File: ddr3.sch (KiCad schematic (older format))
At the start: 36 parts, among them U7 AS4C256M16D3, U8 TPS51200DRC

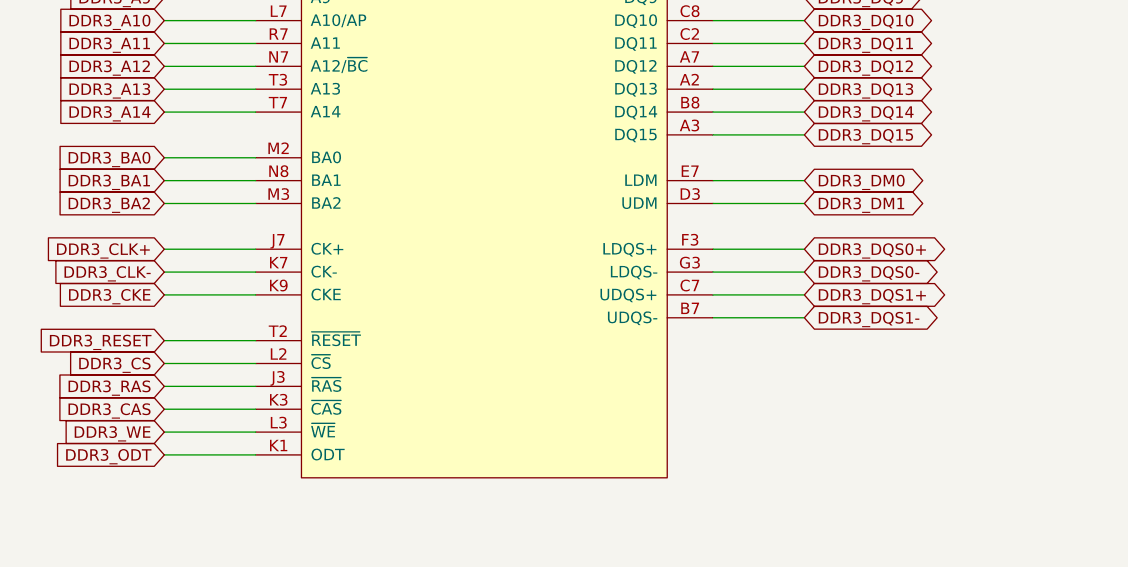
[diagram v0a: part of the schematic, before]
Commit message: DDR routing in progress
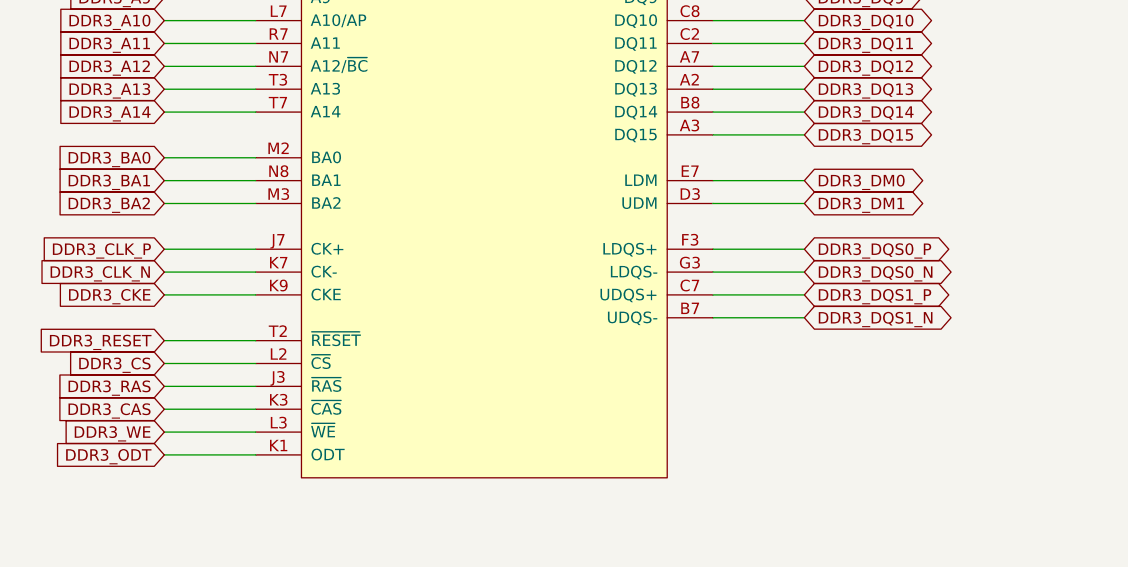
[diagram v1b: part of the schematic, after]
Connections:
- net DDR3_CLK+: no longer U7.J7 (CK+)
- net DDR3_CLK-: no longer U7.K7 (CK-)
- net DDR3_DQS0+ renamed DDR3_DQS0_P
- net DDR3_DQS0- renamed DDR3_DQS0_N
- net DDR3_DQS1+ renamed DDR3_DQS1_P
- net DDR3_DQS1- renamed DDR3_DQS1_N
- new net DDR3_CLK_N: U7.K7 (CK-)
- new net DDR3_CLK_P: U7.J7 (CK+)
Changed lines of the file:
@@
 DDR3_BA2
 Text GLabel 3650 4625 0    50   Input ~ 0
-DDR3_CLK+
+DDR3_CLK_P
 Text GLabel 3650 4725 0    50   Input ~ 0
-DDR3_CLK-
+DDR3_CLK_N
 Text GLabel 3650 4825 0    50   Input ~ 0
 DDR3_CKE
@@
 	6050 4425 6450 4425
 Text GLabel 6450 4625 2    50   BiDi ~ 0
-DDR3_DQS0+
+DDR3_DQS0_P
 Text GLabel 6450 4725 2    50   BiDi ~ 0
-DDR3_DQS0-
+DDR3_DQS0_N
 Text GLabel 6450 4825 2    50   BiDi ~ 0
-DDR3_DQS1+
+DDR3_DQS1_P
 Text GLabel 6450 4925 2    50   BiDi ~ 0
-DDR3_DQS1-
+DDR3_DQS1_N
 Wire Wire Line
 	6450 4625 6050 4625

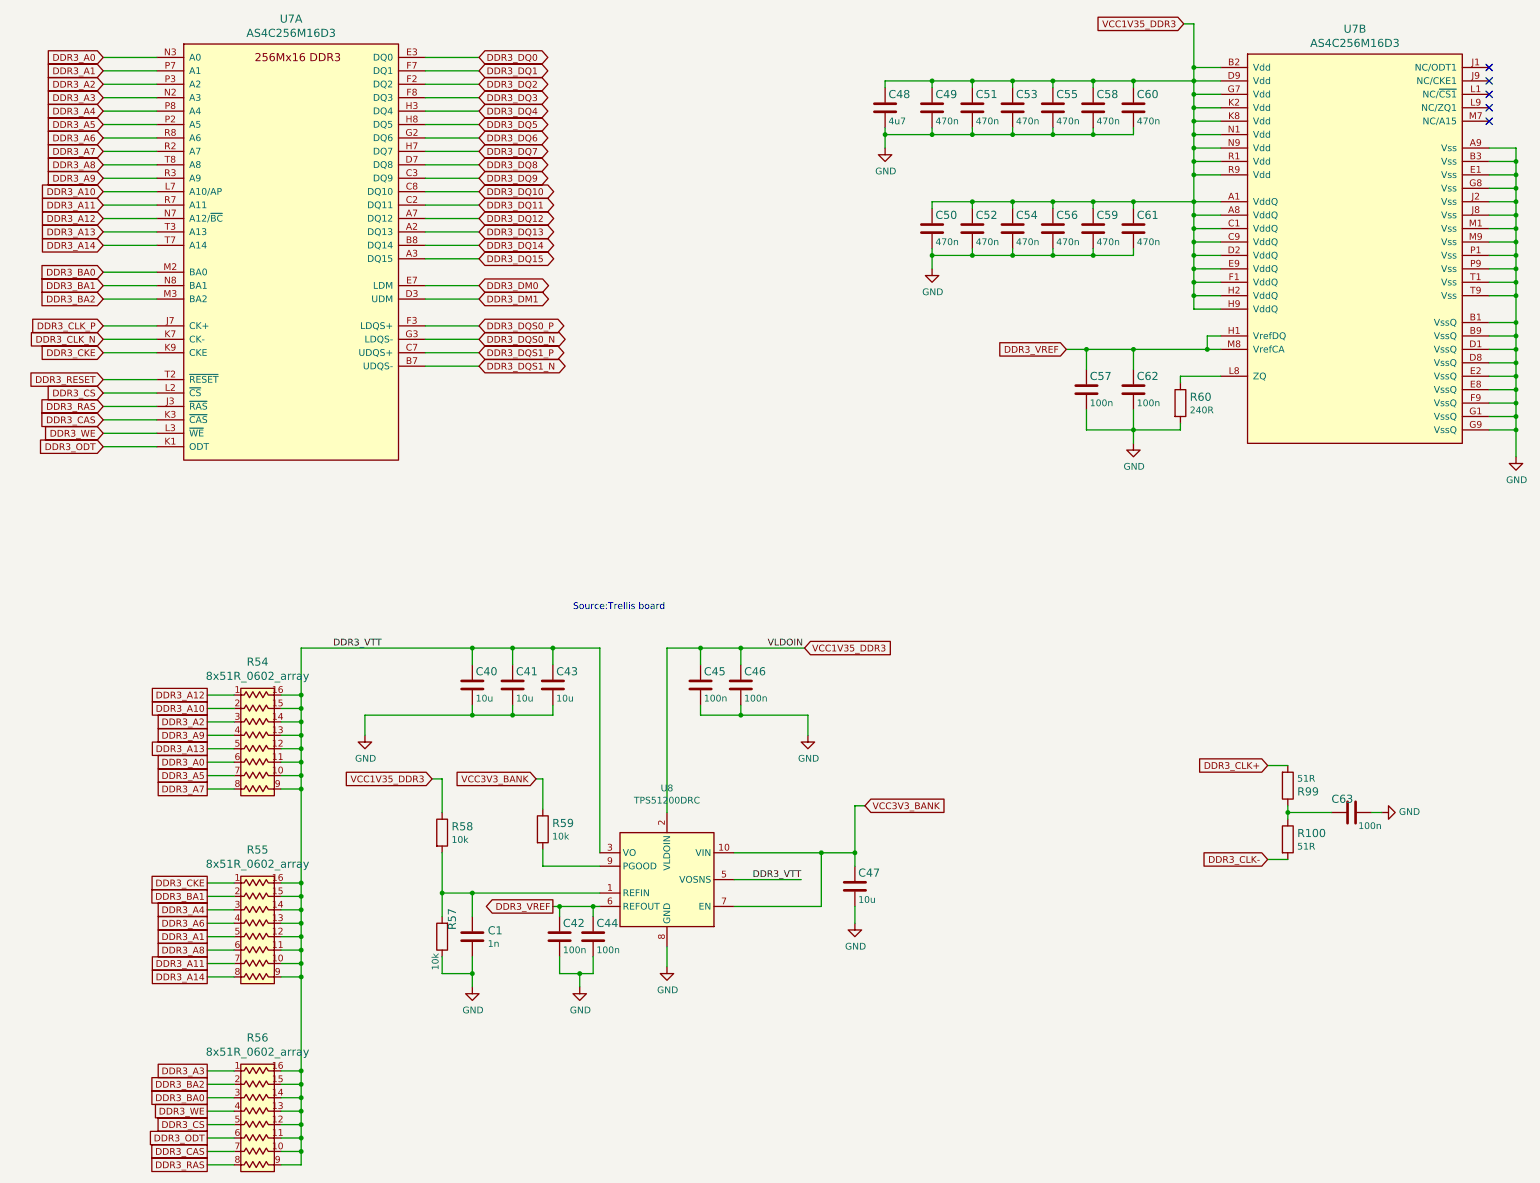
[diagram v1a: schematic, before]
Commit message: Add filtering caps to DDR
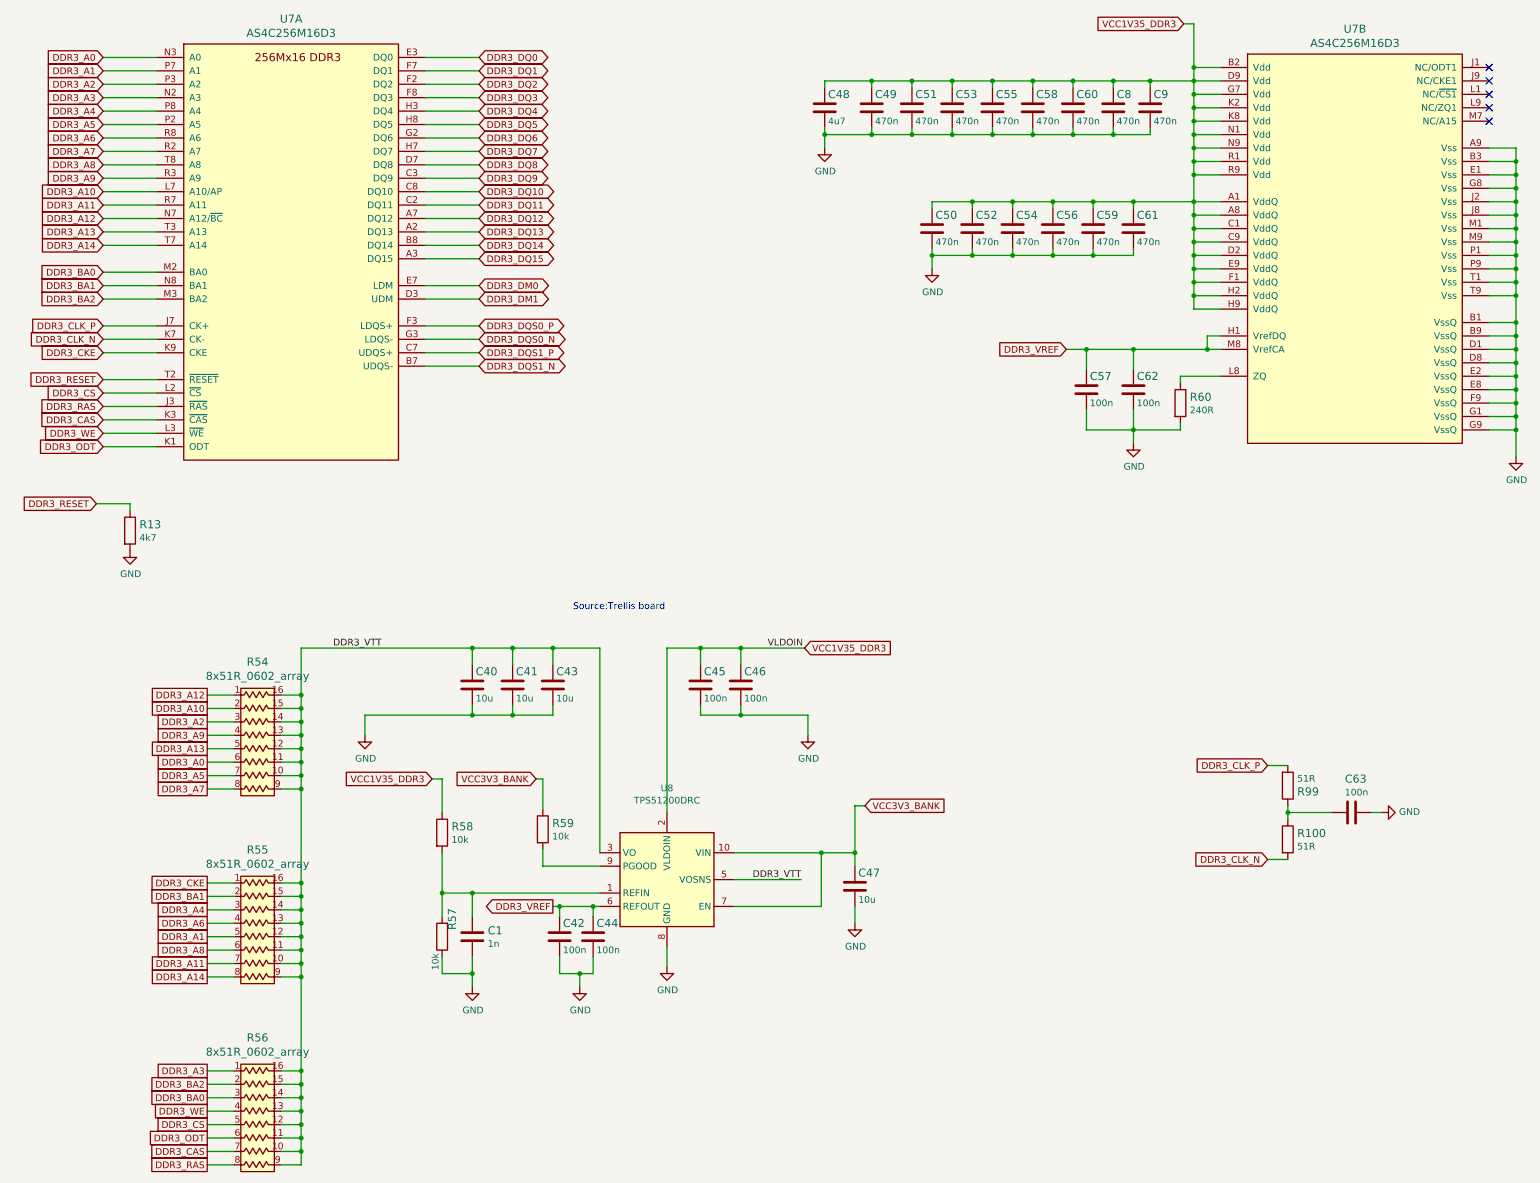
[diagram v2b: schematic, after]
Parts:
- added C8, C9: C_470n_0402, artix-dc-scm-footprints:0402-cap, symbol artix-dc-scm:C_470n_0402
- added R13: R_4k7_0402, antmicro-footprints:0402-res, symbol antmicroResistors0402:R_4k7_0402
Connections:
- net DDR3_CLK+ is gone; now on net DDR3_CLK_P: R99.2
- net DDR3_CLK- is gone; now on net DDR3_CLK_N: R100.2
- net DDR3_RESET: now also R13.1
- net GND: now also C8.2, C9.2, R13.2
- net VCC1V35_DDR3: now also C8.1, C9.1
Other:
- moved on the sheet: C48, C49, C51, C53, C55, C58, C60

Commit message: Updated voltage supply labels, connected gpios left
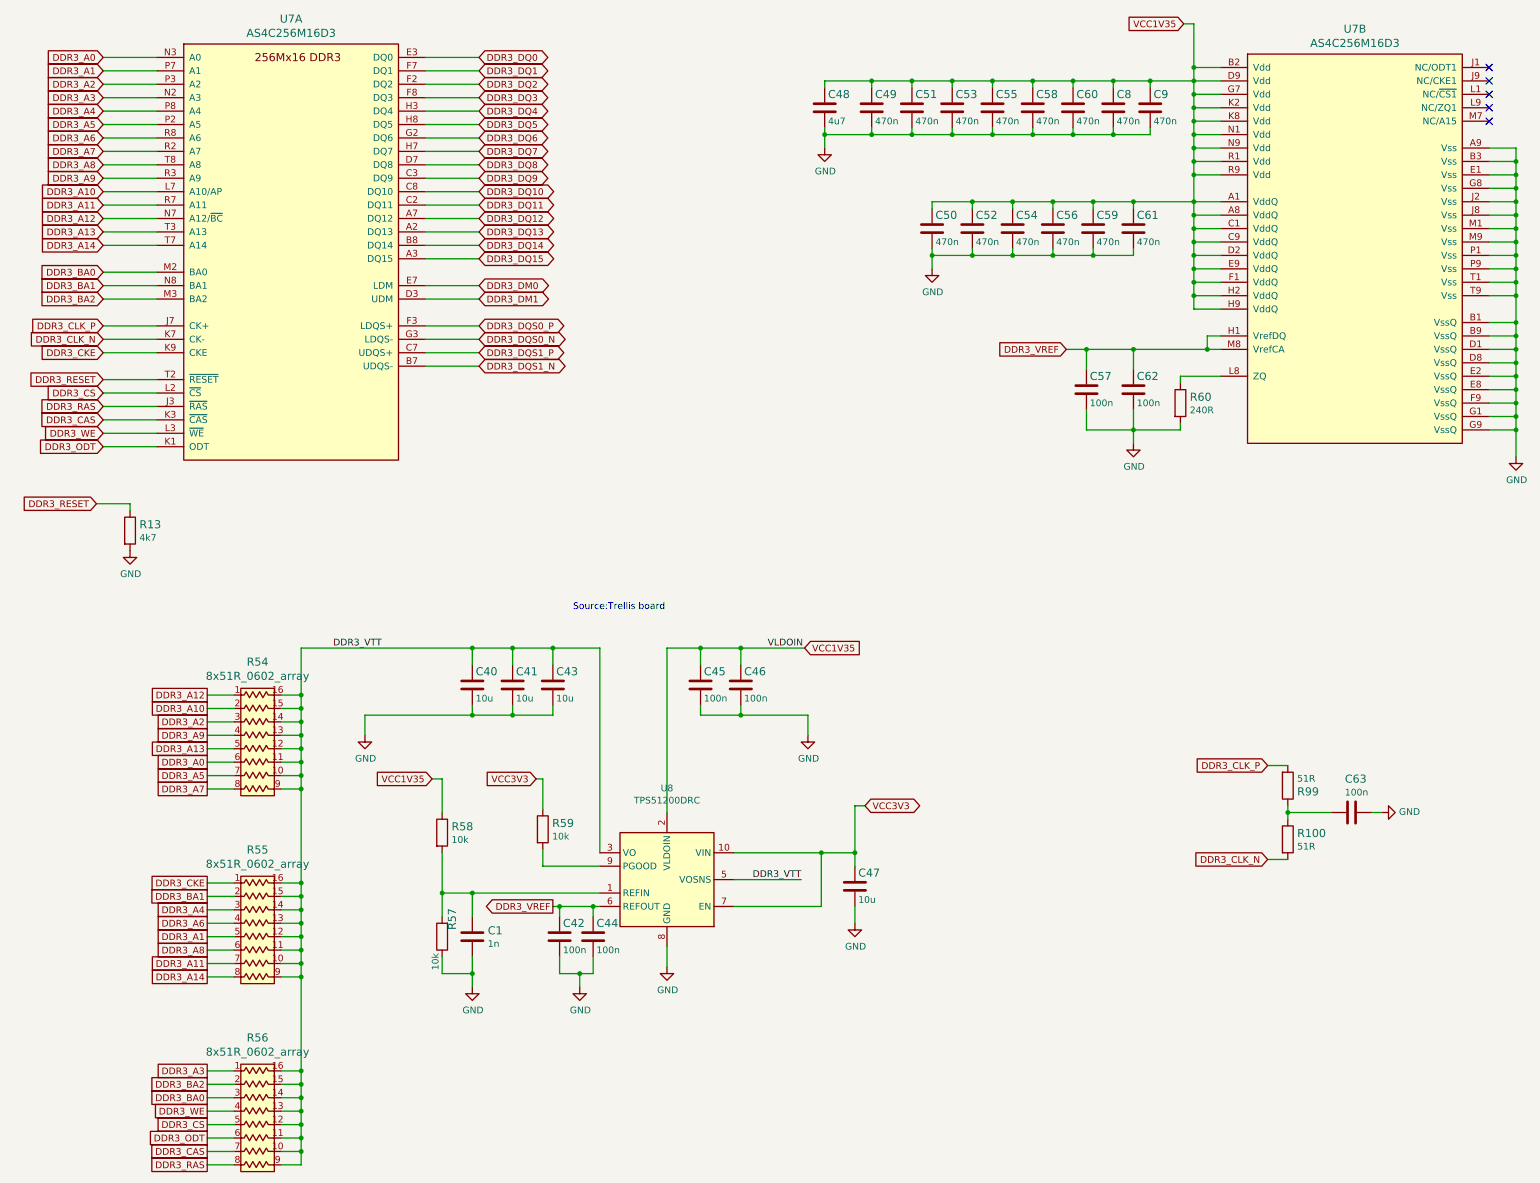
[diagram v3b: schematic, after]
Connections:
- net VCC1V35_DDR3 renamed VCC1V35
- net VCC3V3_BANK renamed VCC3V3
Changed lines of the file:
@@
 Connection ~ 6175 8850
 Text GLabel 8875 7025 2    50   Input ~ 0
-VCC1V35_DDR3
+VCC1V35
 Text GLabel 11700 2375 0    50   Input ~ 0
-VCC1V35_DDR3
-Text GLabel 6100 8000 0    50   Input ~ 0
-VCC1V35_DDR3
-Text GLabel 6875 8000 0    50   Input ~ 0
-VCC3V3_BANK
-Text GLabel 9325 8200 2    50   Input ~ 0
-VCC3V3_BANK
+VCC1V35
+Text GLabel 9325 8200 2    50   3State ~ 0
+VCC3V3
 Wire Wire Line
 	8350 8950 9000 8950
@@
 Wire Wire Line
 	11450 2850 11450 2800
+Text GLabel 6875 8000 0    50   Input ~ 0
+VCC3V3
+Text GLabel 6100 8000 0    50   Input ~ 0
+VCC1V35
 $EndSCHEMATC

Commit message: Updated local libs
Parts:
- R13: footprint antmicro-footprints:0402-res -> artix-dc-scm-footprints:0402-res; symbol antmicroResistors0402:R_4k7_0402 -> artix-dc-scm:R_4k7_0402
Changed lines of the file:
@@
 $EndComp
 $Comp
-L antmicroResistors0402:R_4k7_0402 R13
+L artix-dc-scm:R_4k7_0402 R13
 U 1 1 5FF6FE54
 P 3850 6150
 F 0 "R13" V 3805 6220 60  0000 L CNN
 F 1 "R_4k7_0402" H 3850 6000 60  0001 C CNN
-F 2 "antmicro-footprints:0402-res" H 4050 6350 60  0001 L CNN
+F 2 "artix-dc-scm-footprints:0402-res" H 4050 6350 60  0001 L CNN
 F 3 "" H 3850 6150 50  0001 C CNN
 F 4 "PANASONIC_ELECTRONIC_COMPONENTS" H 4050 6550 60  0001 L CNN "Manufacturer"

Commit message: Update DDR3 termination
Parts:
- removed R54, R55, R56: 8x51R_0602_array, artix-dc-scm-footprints:R_Array_Convex_8x0602, symbol artix-dc-scm:8x51R_0602_array
- added R162, R163, R164, R167, R168, R169, R170, R171, R172, R173, R174, R175, R176, R177, R178, R179, R180, R181, R182, R183, R184, R54, R55, R56: R_51R_0402, antmicro-footprints:0402-res, symbol antmicroResistors0402:R_51R_0402
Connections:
- net DDR3_A0: now also R168.1
- net DDR3_A1: now also R175.1
- net DDR3_A10: now also R183.1
- net DDR3_A11: now also R176.1
- net DDR3_A12: now also R174.1
- net DDR3_A13: now also R173.1
- net DDR3_A14: now also R177.1
- net DDR3_A2: now also R169.1
- net DDR3_A3: now also R167.1
- net DDR3_A4: now also R178.1
- net DDR3_A5: now also R172.1
- net DDR3_A6: now also R179.1
- net DDR3_A7: now also R170.1
- net DDR3_A8: now also R180.1
- net DDR3_A9: now also R171.1
- net DDR3_BA0: now also R163.1
- net DDR3_BA1: now also R181.1
- net DDR3_BA2: now also R164.1
- net DDR3_CAS: now also R55.1
- net DDR3_CKE: now also R182.1
- net DDR3_CS: now also R184.1
- net DDR3_ODT: now also R56.1
- net DDR3_RAS: now also R54.1
- net DDR3_VTT: now also R162.2, R163.2, R164.2, R167.2, R168.2, R169.2, R170.2, R171.2, R172.2, R173.2, R174.2, R175.2, R176.2, R177.2, R178.2, R179.2, R180.2, R181.2, R182.2, R183.2, R184.2, R54.2, R55.2, R56.2
- net DDR3_WE: now also R162.1

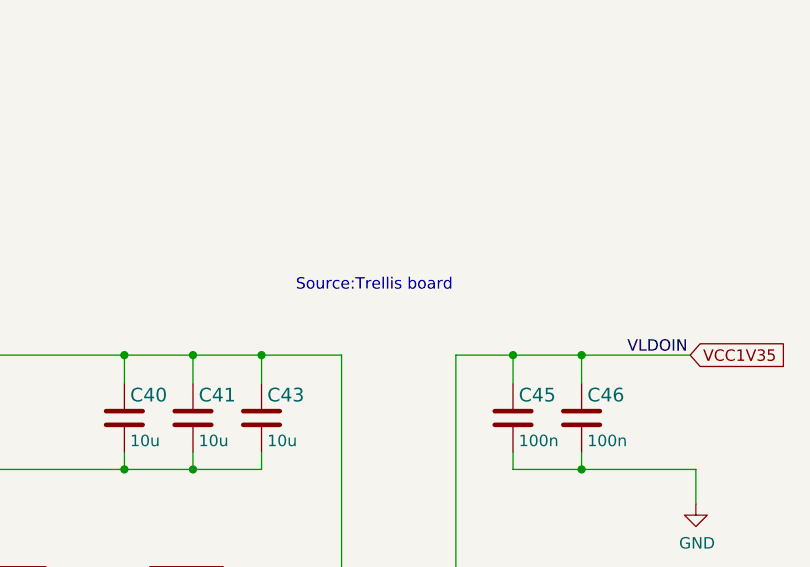
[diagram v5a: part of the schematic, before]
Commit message: Update schematic notes, update SPI0 connection
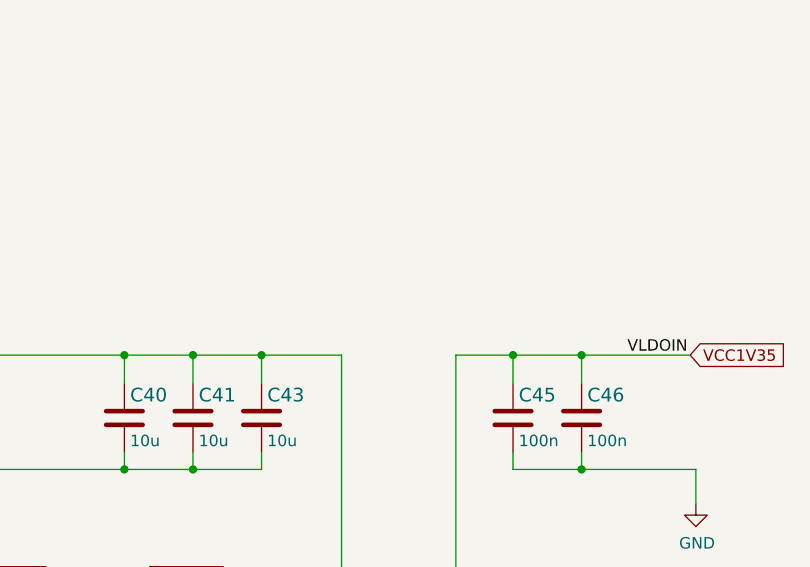
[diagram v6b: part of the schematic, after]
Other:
- note removed: "Source:Trellis board"
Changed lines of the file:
@@
 Wire Wire Line
 	7850 7025 7850 8250
-Text Notes 7150 6750 0    50   ~ 0
-Source:Trellis board
 $Comp
 L artix-dc-scm:C_10u_0402 C47
